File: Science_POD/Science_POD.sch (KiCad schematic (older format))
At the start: 10 parts, among them U1 Molex_SL_2, U2 AP1059, U3 ESP_8266_Breakout_Small, U4 Molex_SL_3, U5 Molex_SL_2

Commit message: finalised board
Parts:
- added R2: 10K, Resistors_SMD:R_0603_HandSoldering, symbol R
- R1: value 100 -> 10K
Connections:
- net Ain: now also R2.1; no longer U3.7 (Rx)
- new net: R2.2, U3.7 (Rx)
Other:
- note added: "(.5-1)*3.3V"
- note removed: "(.25-1)*3.3V"
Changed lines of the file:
@@
 Text Notes 6900 3700 0    60   ~ 0
 Thermister
-Text Notes 6850 2900 0    60   ~ 0
+Text Notes 7000 2950 0    60   ~ 0
 Moisture
 $Comp
@@
 P 6900 4100
 F 0 "R1" V 6980 4100 50  0000 C CNN
-F 1 "100" V 6900 4100 50  0000 C CNN
+F 1 "10K" V 6900 4100 50  0000 C CNN
 F 2 "Resistors_SMD:R_0603_HandSoldering" V 6830 4100 50  0001 C CNN
 F 3 "" H 6900 4100 50  0001 C CNN
@@
 GND
 Text Notes 7250 3950 0    60   ~ 0
-(.25-1)*3.3V
+(.5-1)*3.3V
 Wire Wire Line
 	4750 2650 4750 2150
@@
 Wire Wire Line
 	5000 3800 5000 4050
-Wire Wire Line
-	5000 4050 6200 4050
 Wire Wire Line
 	6900 3950 6200 3950
@@
 Wire Wire Line
 	5950 3100 5100 3100
+$Comp
+L R R2
+U 1 1 5AB93F80
+P 5650 4050
+F 0 "R2" V 5730 4050 50  0000 C CNN
+F 1 "10K" V 5650 4050 50  0000 C CNN
+F 2 "Resistors_SMD:R_0603_HandSoldering" V 5580 4050 50  0001 C CNN
+F 3 "" H 5650 4050 50  0001 C CNN
+	1    5650 4050
+	0    1    1    0
+$EndComp
+Wire Wire Line
+	5800 4050 6200 4050
+Wire Wire Line
+	5000 4050 5500 4050
 $EndSCHEMATC

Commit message: Generated Final Gerbs
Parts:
- added D2: LED, Diodes_SMD:D_1206, symbol LED
- added R3: 330, Resistors_SMD:R_0603_HandSoldering, symbol R
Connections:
- net +3V3: now also R3.1
- net GND: now also D2.1 (K)
- new net: D2.2 (A), R3.2
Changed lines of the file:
@@
 Wire Wire Line
 	5000 4050 5500 4050
+$Comp
+L R R3
+U 1 1 5ABAE27A
+P 4950 2800
+F 0 "R3" V 5030 2800 50  0000 C CNN
+F 1 "330" V 4950 2800 50  0000 C CNN
+F 2 "Resistors_SMD:R_0603_HandSoldering" V 4880 2800 50  0001 C CNN
+F 3 "" H 4950 2800 50  0001 C CNN
+	1    4950 2800
+	-1   0    0    1
+$EndComp
+$Comp
+L LED D2
+U 1 1 5ABAE2C5
+P 4950 2400
+F 0 "D2" H 4950 2500 50  0000 C CNN
+F 1 "LED" H 4950 2300 50  0000 C CNN
+F 2 "Diodes_SMD:D_1206" H 4950 2400 50  0001 C CNN
+F 3 "" H 4950 2400 50  0001 C CNN
+	1    4950 2400
+	0    1    1    0
+$EndComp
+Wire Wire Line
+	4950 2250 4950 2150
+Connection ~ 4950 2150
+Wire Wire Line
+	4950 2550 4950 2650
+Wire Wire Line
+	4950 2950 4950 3200
+Connection ~ 4950 3200
 $EndSCHEMATC

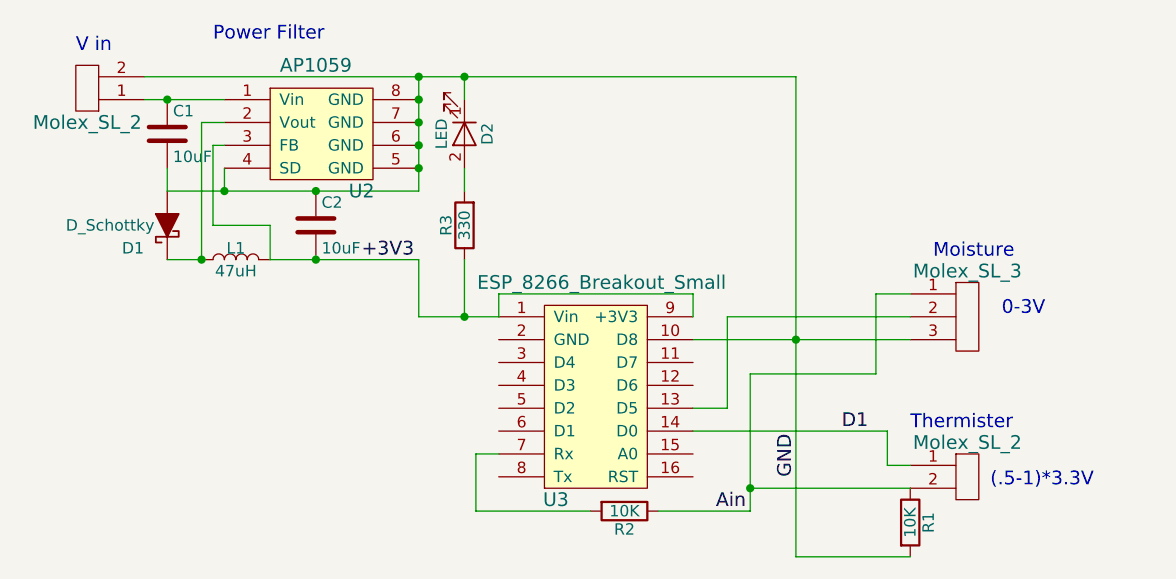
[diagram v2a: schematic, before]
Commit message: Rev 2-added SL-3 for thermister. Fixed esp footprint
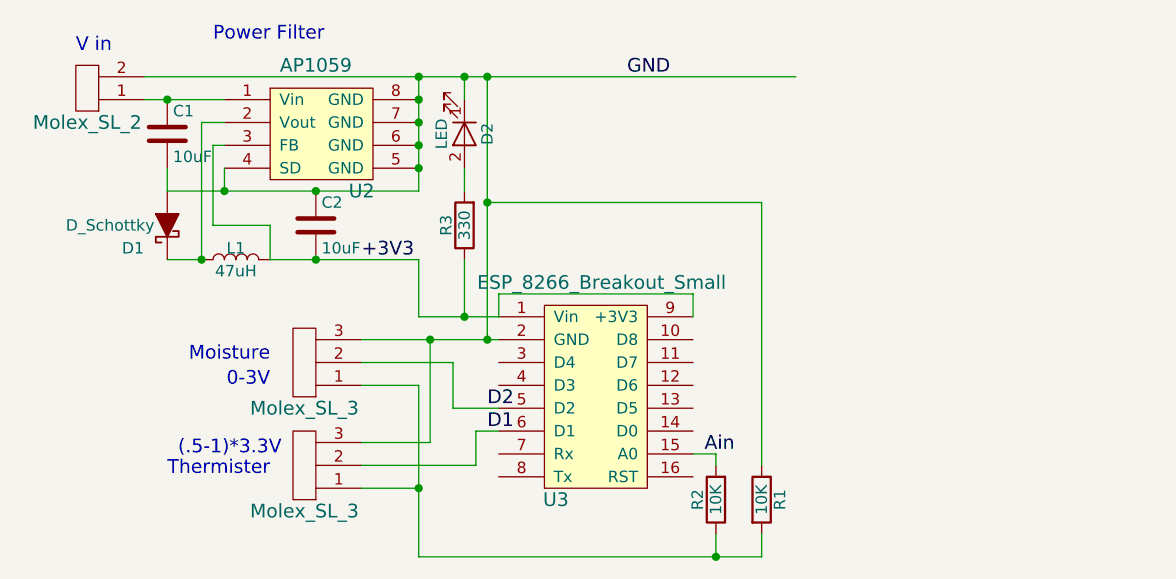
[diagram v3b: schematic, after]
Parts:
- removed U5: Molex_SL_2, MRDT_Connectors:MOLEX_SL_2, symbol Molex_SL_2
- added U5: Molex_SL_3, MRDT_Connectors:MOLEX_SL_3, symbol Molex_SL_3
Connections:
- net Ain: now also R2.2, U3.15 (A0); no longer R1.1, R2.1, U4.1
- net D1: now also U3.6 (D1), U5.2; no longer U3.14 (D0)
- net GND: now also R1.1, U3.2 (GND), U5.3; no longer R1.2, U3.10 (D8)
- net at U3.13 (D5): no longer U4.2
- net D2: now reaches U3.5 (D2)
- net D2: now also U4.2
- net at U3.7 (Rx): no longer R2.2
- new net: R1.2, R2.1, U4.1, U5.1
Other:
- moved on the sheet: R1, R2
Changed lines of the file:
@@
-$EndComp
-$Comp
-L Molex_SL_2 U5
-U 1 1 5AB45C51
-P 7100 4000
-F 0 "U5" H 7150 3950 60  0001 C CNN
-F 1 "Molex_SL_2" H 7150 4250 60  0000 C CNN
-F 2 "MRDT_Connectors:MOLEX_SL_2" H 7100 3900 60  0001 C CNN
-F 3 "" H 7100 3900 60  0001 C CNN
-	1    7100 4000
-	1    0    0    -1
 $EndComp
 $Comp
 L Molex_SL_3 U4
 U 1 1 5AB45D3D
-P 7100 3350
-F 0 "U4" H 7150 3300 60  0001 C CNN
-F 1 "Molex_SL_3" H 7150 3700 60  0000 C CNN
-F 2 "MRDT_Connectors:MOLEX_SL_3" H 7100 3350 60  0001 C CNN
-F 3 "" H 7100 3350 60  0001 C CNN
-	1    7100 3350
-	1    0    0    -1
-$EndComp
-Text Notes 6900 3700 0    60   ~ 0
+P 4300 3250
+F 0 "U4" H 4350 3200 60  0001 C CNN
+F 1 "Molex_SL_3" H 4350 3600 60  0000 C CNN
+F 2 "MRDT_Connectors:MOLEX_SL_3" H 4300 3250 60  0001 C CNN
+F 3 "" H 4300 3250 60  0001 C CNN
+	1    4300 3250
+	-1   0    0    1
+$EndComp
+Text Notes 4100 3900 2    60   ~ 0
 Thermister
-Text Notes 7000 2950 0    60   ~ 0
+Text Notes 4100 3400 2    60   ~ 0
 Moisture
 $Comp
 L R R1
 U 1 1 5AB45F03
-P 6900 4100
-F 0 "R1" V 6980 4100 50  0000 C CNN
-F 1 "10K" V 6900 4100 50  0000 C CNN
-F 2 "Resistors_SMD:R_0603_HandSoldering" V 6830 4100 50  0001 C CNN
-F 3 "" H 6900 4100 50  0001 C CNN
-	1    6900 4100
+P 6250 4000
+F 0 "R1" V 6330 4000 50  0000 C CNN
+F 1 "10K" V 6250 4000 50  0000 C CNN
+F 2 "Resistors_SMD:R_0603_HandSoldering" V 6180 4000 50  0001 C CNN
+F 3 "" H 6250 4000 50  0001 C CNN
+	1    6250 4000
 	1    0    0    -1
 $EndComp
 Text Label 4500 2950 0    60   ~ 0
 +3V3
-Text Label 6050 4050 0    60   ~ 0
+Text Label 6000 3800 0    60   ~ 0
 Ain
-Text Label 6600 3700 0    60   ~ 0
+Text Label 5050 3700 0    60   ~ 0
 D1
-Text Label 6400 3900 1    60   ~ 0
+Text Label 5850 2150 2    60   ~ 0
 GND
-Text Notes 7250 3950 0    60   ~ 0
+Text Notes 4150 3810 2    60   ~ 0
 (.5-1)*3.3V
-Wire Wire Line
-	4750 2650 4750 2150
-Connection ~ 4750 2350
-Connection ~ 4750 2450
-Wire Wire Line
-	3550 2250 3900 2250
-Wire Wire Line
-	3550 2150 6400 2150
-Connection ~ 4750 2250
-Connection ~ 4750 2150
-Wire Wire Line
-	3900 2550 3900 2650
-Wire Wire Line
-	3650 2650 4750 2650
-Connection ~ 4750 2550
-Connection ~ 3900 2650
-Wire Wire Line
-	3800 2350 3900 2350
-Wire Wire Line
-	3650 2650 3650 2550
-Connection ~ 3650 2250
-Wire Wire Line
-	3800 2350 3800 2950
-Connection ~ 3800 2950
-Wire Wire Line
-	3800 2950 3650 2950
-Wire Wire Line
-	3900 2450 3850 2450
-Wire Wire Line
-	3850 2450 3850 2800
-Wire Wire Line
-	3850 2800 4100 2800
-Wire Wire Line
-	4100 2800 4100 2950
-Wire Wire Line
-	4100 2950 4750 2950
-Connection ~ 4300 2950
-Wire Wire Line
-	5950 3700 6800 3700
-Wire Wire Line
-	6900 3850 6800 3850
-Wire Wire Line
-	6800 3850 6800 3700
-Wire Wire Line
-	5100 3800 5000 3800
-Wire Wire Line
-	5000 3800 5000 4050
-Wire Wire Line
-	6900 3950 6200 3950
-Connection ~ 6200 3950
-Wire Wire Line
-	6400 2150 6400 4250
-Wire Wire Line
-	6400 4250 6900 4250
-Wire Wire Line
-	4750 2950 4750 3200
-Wire Wire Line
-	4750 3200 5100 3200
-Wire Wire Line
-	5100 3200 5100 3100
-Connection ~ 6400 3300
-Wire Wire Line
-	6100 3200 6100 3600
-Wire Wire Line
-	6100 3600 5950 3600
-Wire Wire Line
-	5950 3300 6900 3300
-Wire Wire Line
-	6900 3200 6100 3200
-Wire Wire Line
-	6200 4050 6200 3450
-Wire Wire Line
-	6200 3450 6750 3450
-Wire Wire Line
-	6750 3450 6750 3100
-Wire Wire Line
-	6750 3100 6900 3100
-Text Notes 7300 3200 0    60   ~ 0
+Text Notes 4100 3510 2    60   ~ 0
 0-3V
 $Comp
@@
 	1    0    0    -1
 $EndComp
-Connection ~ 4300 2650
-Wire Wire Line
-	5950 3200 5950 3100
-Wire Wire Line
-	5950 3100 5100 3100
 $Comp
 L R R2
 U 1 1 5AB93F80
-P 5650 4050
-F 0 "R2" V 5730 4050 50  0000 C CNN
-F 1 "10K" V 5650 4050 50  0000 C CNN
-F 2 "Resistors_SMD:R_0603_HandSoldering" V 5580 4050 50  0001 C CNN
-F 3 "" H 5650 4050 50  0001 C CNN
-	1    5650 4050
-	0    1    1    0
-$EndComp
-Wire Wire Line
-	5800 4050 6200 4050
-Wire Wire Line
-	5000 4050 5500 4050
+P 6050 4000
+F 0 "R2" V 6130 4000 50  0000 C CNN
+F 1 "10K" V 6050 4000 50  0000 C CNN
+F 2 "Resistors_SMD:R_0603_HandSoldering" V 5980 4000 50  0001 C CNN
+F 3 "" H 6050 4000 50  0001 C CNN
+	1    6050 4000
+	-1   0    0    1
+$EndComp
 $Comp
 L R R3
@@
 $EndComp
 Wire Wire Line
+	4750 2650 4750 2150
+Connection ~ 4750 2350
+Connection ~ 4750 2450
+Wire Wire Line
+	3550 2250 3900 2250
+Wire Wire Line
+	3550 2150 6400 2150
+Connection ~ 4750 2250
+Connection ~ 4750 2150
+Wire Wire Line
+	3900 2550 3900 2650
+Wire Wire Line
+	3650 2650 4750 2650
+Connection ~ 4750 2550
+Connection ~ 3900 2650
+Wire Wire Line
+	3800 2350 3900 2350
+Wire Wire Line
+	3650 2650 3650 2550
+Connection ~ 3650 2250
+Wire Wire Line
+	3800 2350 3800 2950
+Connection ~ 3800 2950
+Wire Wire Line
+	3800 2950 3650 2950
+Wire Wire Line
+	3900 2450 3850 2450
+Wire Wire Line
+	3850 2450 3850 2800
+Wire Wire Line
+	3850 2800 4100 2800
+Wire Wire Line
+	4100 2800 4100 2950
+Wire Wire Line
+	4100 2950 4750 2950
+Connection ~ 4300 2950
+Wire Wire Line
+	4750 2950 4750 3200
+Wire Wire Line
+	4750 3200 5100 3200
+Wire Wire Line
+	5100 3200 5100 3100
+Connection ~ 4300 2650
+Wire Wire Line
+	5950 3200 5950 3100
+Wire Wire Line
+	5950 3100 5100 3100
+Wire Wire Line
 	4950 2250 4950 2150
 Connection ~ 4950 2150
@@
 	4950 2950 4950 3200
 Connection ~ 4950 3200
+Wire Wire Line
+	4500 3300 5100 3300
+Wire Wire Line
+	5050 3300 5050 2150
+Connection ~ 5050 2150
+Wire Wire Line
+	4500 3850 5000 3850
+Connection ~ 5050 3300
+Wire Wire Line
+	6050 3800 5950 3800
+Wire Wire Line
+	6050 4250 6050 4150
+Wire Wire Line
+	6050 3800 6050 3850
+Wire Wire Line
+	5000 3700 5100 3700
+Wire Wire Line
+	6250 4250 6250 4150
+Connection ~ 6050 4250
+Wire Wire Line
+	6250 3850 6250 2700
+Wire Wire Line
+	6250 2700 5050 2700
+Connection ~ 5050 2700
+Wire Wire Line
+	5000 3850 5000 3700
+Wire Wire Line
+	4750 3500 4750 4250
+Wire Wire Line
+	4500 3500 4750 3500
+Wire Wire Line
+	4900 3600 5100 3600
+Wire Wire Line
+	4900 3600 4900 3400
+Wire Wire Line
+	4900 3400 4500 3400
+Text Label 5050 3600 0    60   ~ 0
+D2
+Wire Wire Line
+	4750 4250 6250 4250
+$Comp
+L Molex_SL_3 U5
+U 1 1 5ADFD895
+P 4300 3700
+F 0 "U5" H 4350 3650 60  0001 C CNN
+F 1 "Molex_SL_3" H 4350 4050 60  0000 C CNN
+F 2 "MRDT_Connectors:MOLEX_SL_3" H 4300 3700 60  0001 C CNN
+F 3 "" H 4300 3700 60  0001 C CNN
+	1    4300 3700
+	-1   0    0    1
+$EndComp
+Wire Wire Line
+	4500 3950 4750 3950
+Connection ~ 4750 3950
+Wire Wire Line
+	4500 3750 4800 3750
+Wire Wire Line
+	4800 3750 4800 3300
+Connection ~ 4800 3300
 $EndSCHEMATC

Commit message: Generated Gerbs
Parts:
- removed R2: 10K, Resistors_SMD:R_0603_HandSoldering, symbol R
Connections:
- net Ain: now also R1.2, U4.1, U5.1
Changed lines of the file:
@@
-$EndComp
-$Comp
-L R R2
-U 1 1 5AB93F80
-P 6050 4000
-F 0 "R2" V 6130 4000 50  0000 C CNN
-F 1 "10K" V 6050 4000 50  0000 C CNN
-F 2 "Resistors_SMD:R_0603_HandSoldering" V 5980 4000 50  0001 C CNN
-F 3 "" H 6050 4000 50  0001 C CNN
-	1    6050 4000
-	-1   0    0    1
 $EndComp
 $Comp
@@
 	6050 3800 5950 3800
 Wire Wire Line
-	6050 4250 6050 4150
-Wire Wire Line
-	6050 3800 6050 3850
+	6050 3800 6050 4250
 Wire Wire Line
 	5000 3700 5100 3700

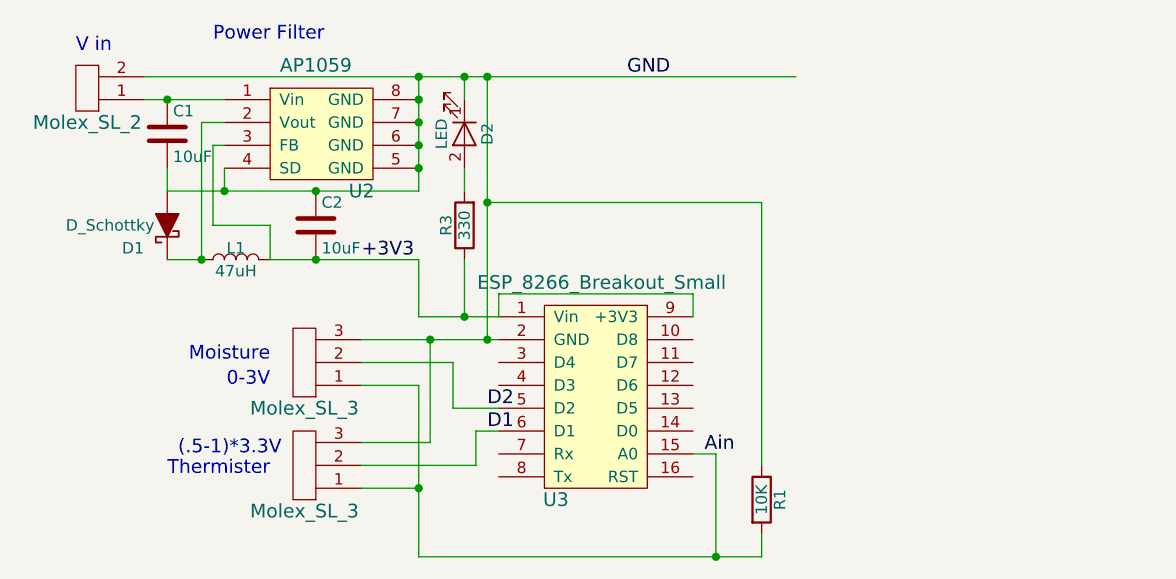
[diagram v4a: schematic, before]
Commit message: Chenged thermister back to SL-2
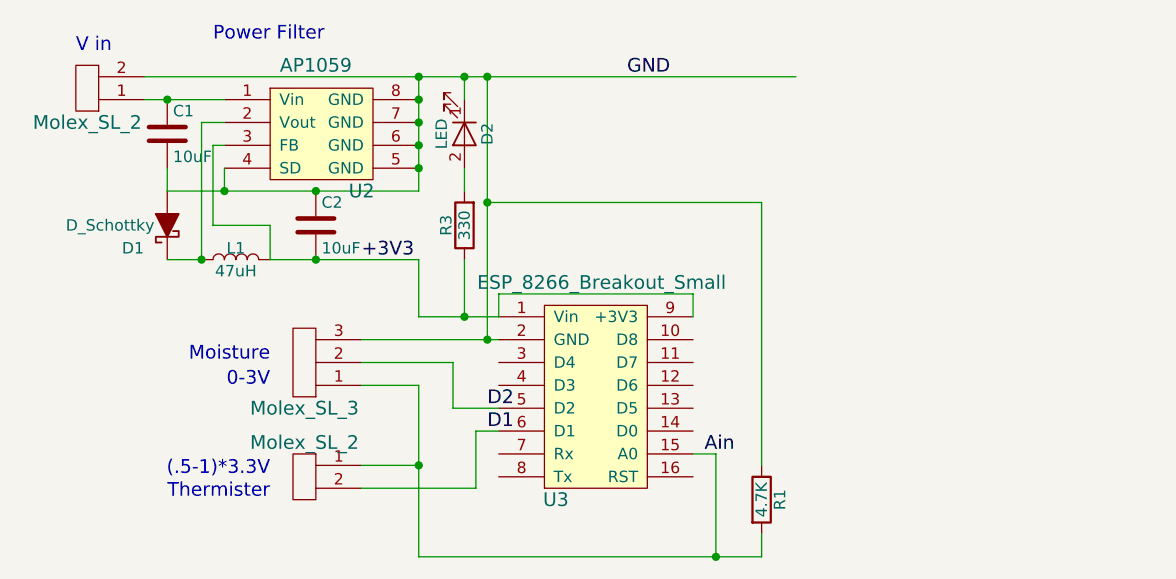
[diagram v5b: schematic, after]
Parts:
- removed U5: Molex_SL_3, MRDT_Connectors:MOLEX_SL_3, symbol Molex_SL_3
- added Conn1: Molex_SL_2, MRDT_Connectors:MOLEX_SL_2_Horizontal, symbol Molex_SL_2
- R1: value 10K -> 4.7K
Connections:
- net Ain: now also Conn1.1
- net D1: now also Conn1.2
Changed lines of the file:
@@
 	-1   0    0    1
 $EndComp
-Text Notes 4100 3900 2    60   ~ 0
+Text Notes 4100 4000 2    60   ~ 0
 Thermister
 Text Notes 4100 3400 2    60   ~ 0
@@
 P 6250 4000
 F 0 "R1" V 6330 4000 50  0000 C CNN
-F 1 "10K" V 6250 4000 50  0000 C CNN
+F 1 "4.7K" V 6250 4000 50  0000 C CNN
 F 2 "Resistors_SMD:R_0603_HandSoldering" V 6180 4000 50  0001 C CNN
 F 3 "" H 6250 4000 50  0001 C CNN
@@
 Text Label 5850 2150 2    60   ~ 0
 GND
-Text Notes 4150 3810 2    60   ~ 0
+Text Notes 4100 3900 2    60   ~ 0
 (.5-1)*3.3V
 Text Notes 4100 3510 2    60   ~ 0
@@
 	5050 3300 5050 2150
 Connection ~ 5050 2150
-Wire Wire Line
-	4500 3850 5000 3850
 Connection ~ 5050 3300
 Wire Wire Line
@@
 Connection ~ 5050 2700
 Wire Wire Line
-	5000 3850 5000 3700
+	5000 3700 5000 3950
 Wire Wire Line
 	4750 3500 4750 4250
@@
 	4750 4250 6250 4250
 $Comp
-L Molex_SL_3 U5
-U 1 1 5ADFD895
-P 4300 3700
-F 0 "U5" H 4350 3650 60  0001 C CNN
-F 1 "Molex_SL_3" H 4350 4050 60  0000 C CNN
-F 2 "MRDT_Connectors:MOLEX_SL_3" H 4300 3700 60  0001 C CNN
-F 3 "" H 4300 3700 60  0001 C CNN
-	1    4300 3700
-	-1   0    0    1
+L Molex_SL_2 Conn1
+U 1 1 5AECCE00
+P 4300 4000
+F 0 "Conn1" H 4350 3950 60  0001 C CNN
+F 1 "Molex_SL_2" H 4350 4250 60  0000 C CNN
+F 2 "MRDT_Connectors:MOLEX_SL_2_Horizontal" H 4300 3900 60  0001 C CNN
+F 3 "" H 4300 3900 60  0001 C CNN
+	1    4300 4000
+	-1   0    0    -1
 $EndComp
 Wire Wire Line
-	4500 3950 4750 3950
-Connection ~ 4750 3950
+	4500 3850 4750 3850
+Connection ~ 4750 3850
 Wire Wire Line
-	4500 3750 4800 3750
-Wire Wire Line
-	4800 3750 4800 3300
-Connection ~ 4800 3300
+	5000 3950 4500 3950
 $EndSCHEMATC
